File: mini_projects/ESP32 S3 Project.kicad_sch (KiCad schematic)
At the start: 17 parts, among them J1 USB_B_Micro, SW1 RESET, SW2 BOOT, U1 ESP32-S3-MINI-1U, U2 D3V3XA4B10LP, U3 TLV75801PDRV

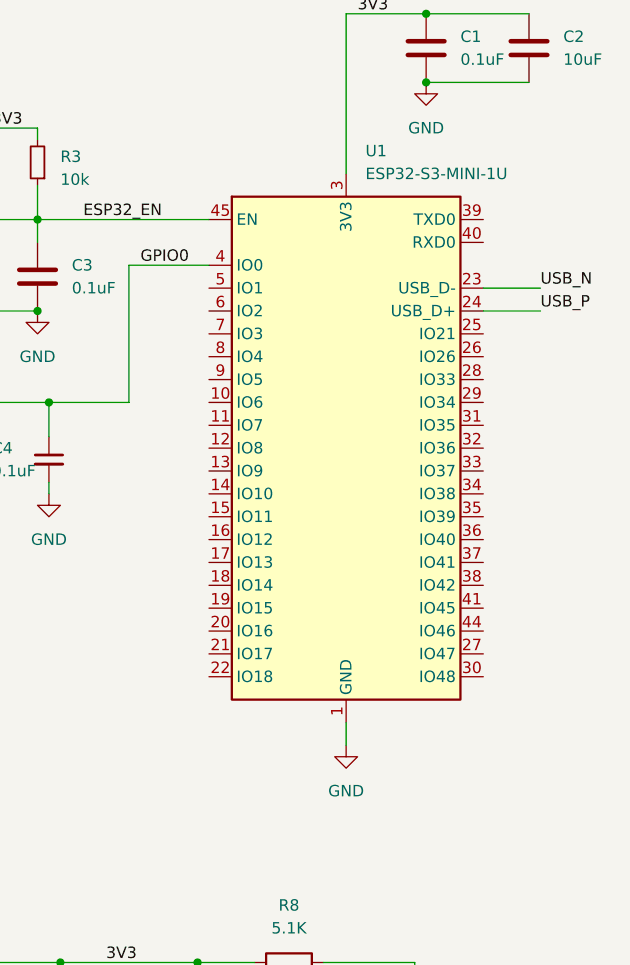
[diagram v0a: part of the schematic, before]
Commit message: Updated the ESP32
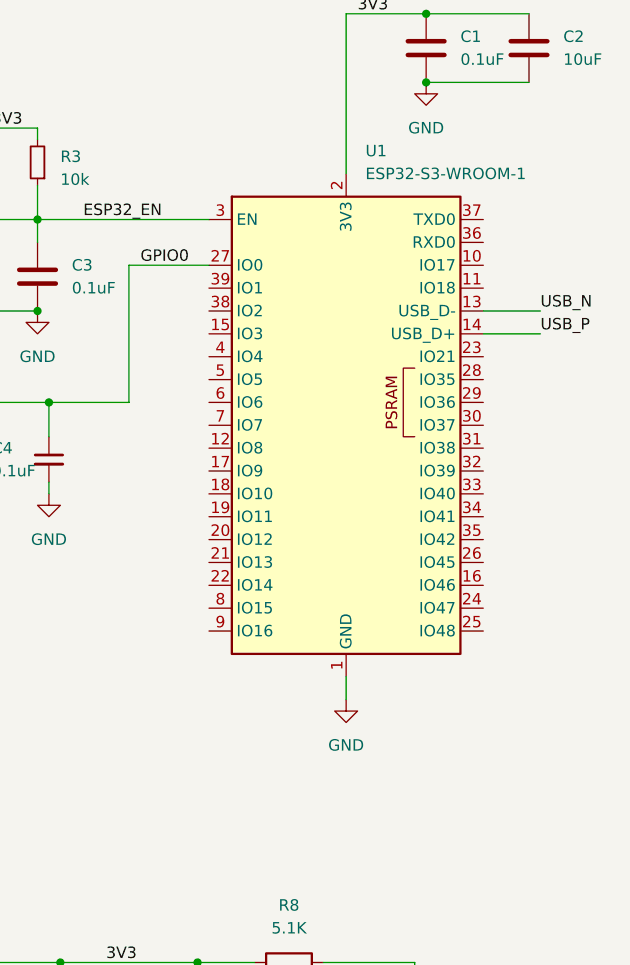
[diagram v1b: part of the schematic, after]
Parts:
- removed U1: ESP32-S3-MINI-1U, RF_Module:ESP32-S2-MINI-1, symbol RF_Module:ESP32-S3-MINI-1U
- added U1: ESP32-S3-WROOM-1, RF_Module:ESP32-S3-WROOM-1, symbol RF_Module:ESP32-S3-WROOM-1
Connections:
- net 3V3: now also U1.2 (3V3)
- net ESP32_EN: now also U1.3 (EN)
- net GND: now also U1.1 (GND), U1.40 (GND), U1.41 (GND)
- net GPIO0: now also U1.27 (IO0)
- net USB_N: now also U1.13 (USB_D-)
- net USB_P: now also U1.14 (USB_D+)
